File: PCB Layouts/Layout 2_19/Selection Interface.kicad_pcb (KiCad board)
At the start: 4 copper layers, 107.5 x 80 mm, 86 parts

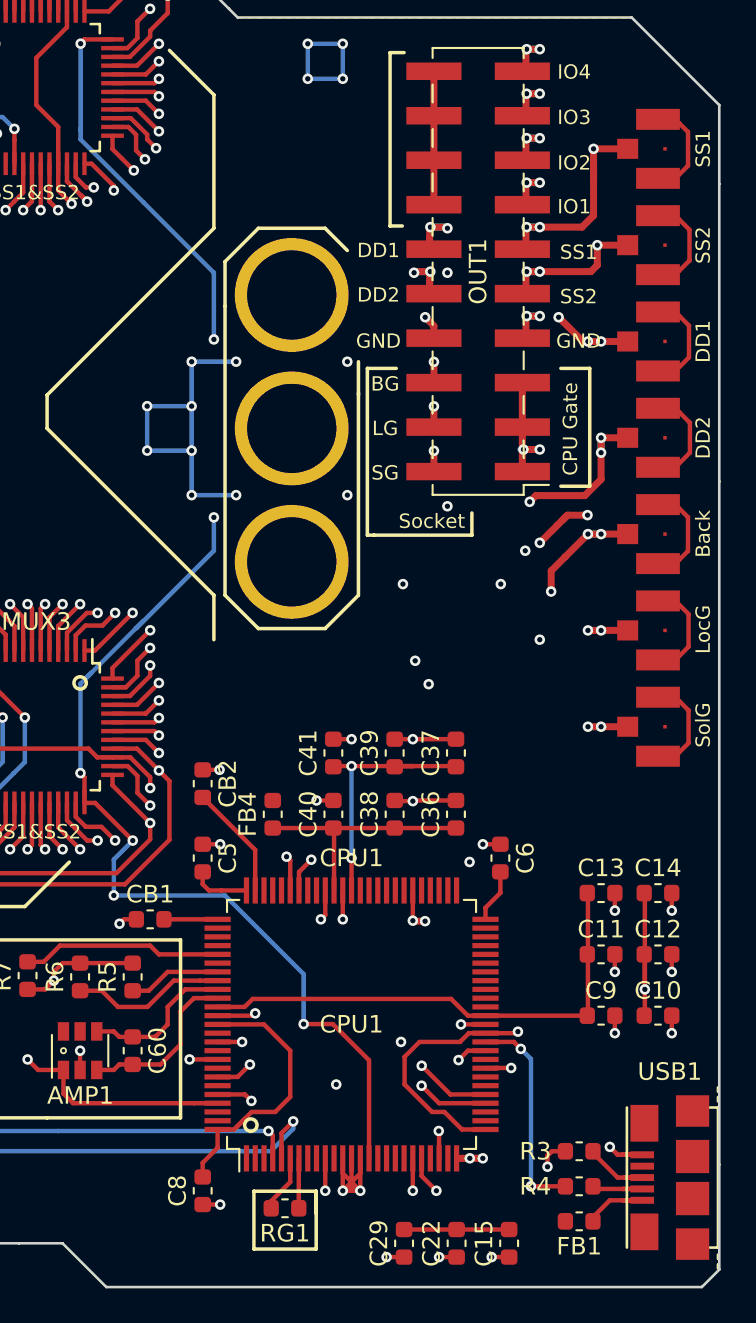
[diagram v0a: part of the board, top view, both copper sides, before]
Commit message: A few more tweaks to Layout 2_19 (very slightly moved up the USB port)
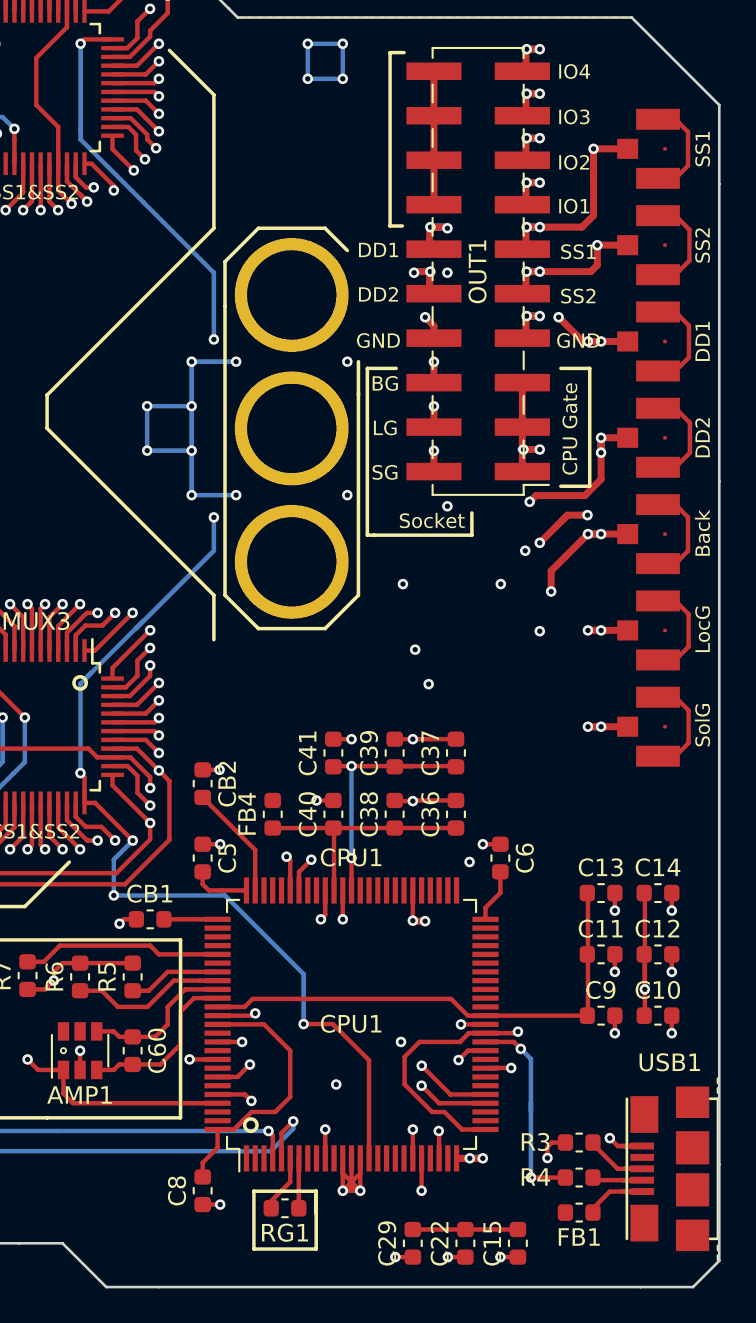
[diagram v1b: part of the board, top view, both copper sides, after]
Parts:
- moved C15 0.50 mm to (248.5, 147.5)
- moved C22 0.50 mm to (245.5, 147.5)
- moved C29 0.50 mm to (242.5, 147.5)
- moved FB1 0.50 mm to (252.0, 145.7)
- moved R3 0.50 mm to (252.0, 141.7)
- moved R4 0.50 mm to (252.0, 143.7)
- moved USB1 0.50 mm to (258.5, 143.2)
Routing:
- net SWDIO5: track 84.6 -> 87.0 mm
- net SWDCLK5: track 93.8 -> 92.6 mm
- net LocalGates_Socket: track 83.2 -> 82.4 mm
- net Gate: track 57.2 -> 56.7 mm
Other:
- outline, holes or cut-outs redrawn

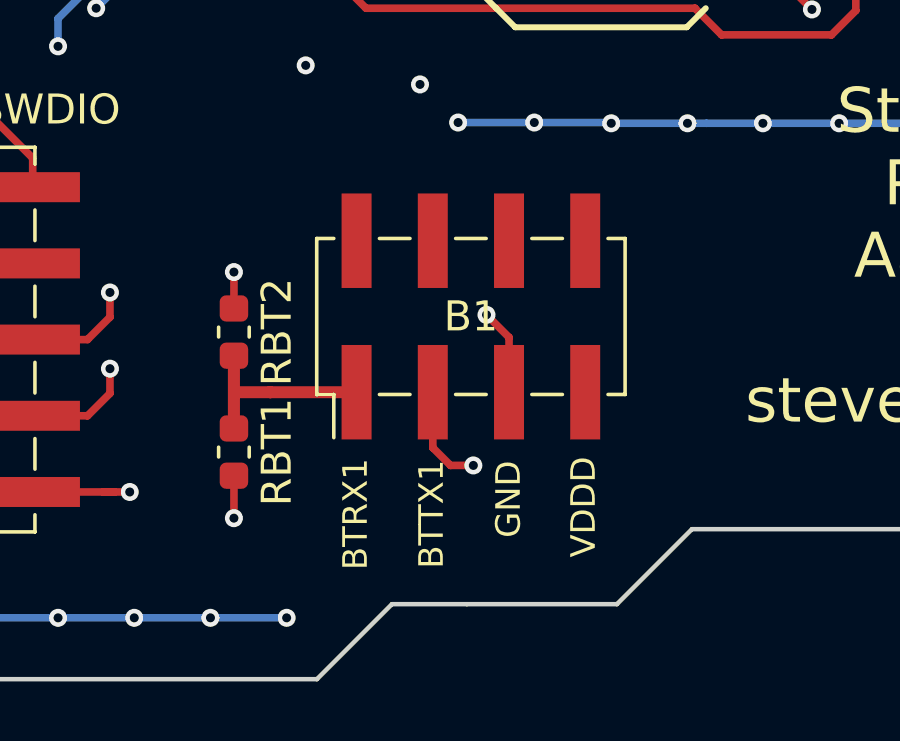
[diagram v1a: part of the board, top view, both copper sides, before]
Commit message: Rotated bluetooth header connector on Layout 2_19
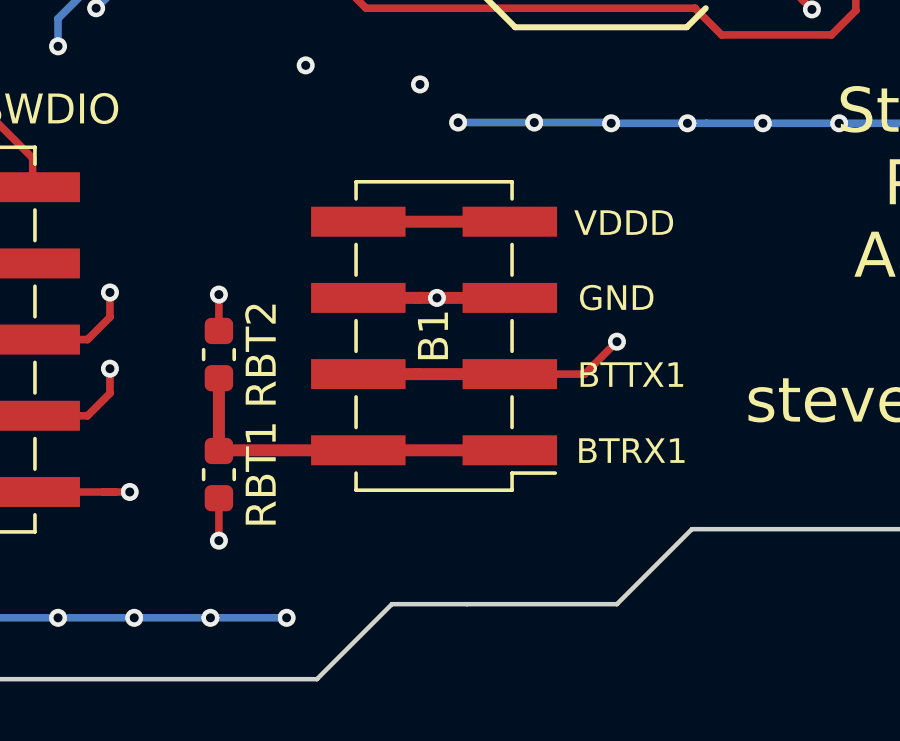
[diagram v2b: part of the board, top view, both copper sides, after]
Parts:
- moved B1 1.39 mm to (178.9, 138.6), turned to 180 degrees
- moved RBT1 0.90 mm to (171.7, 143.2)
- moved RBT2 0.90 mm to (171.7, 139.2)
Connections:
- B1 pad 2: Net-(B1-Pad2) -> BT1_RXR
- B1 pad 4: Net-(B1-Pad4) -> BT1_TX
- B1 pad 6: Net-(B1-Pad6) -> GND
- B1 pad 8: Net-(B1-Pad8) -> VDDD
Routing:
- net BT1_RXR: track 6.56 -> 12.1 mm
- net VDDD: track 130.8 -> 135.8 mm
- net GND: track 428.2 -> 430.3 mm
- net BT1_TX: track 81.1 -> 82.1 mm
- net BT1_RX: track 86.7 -> 87.3 mm

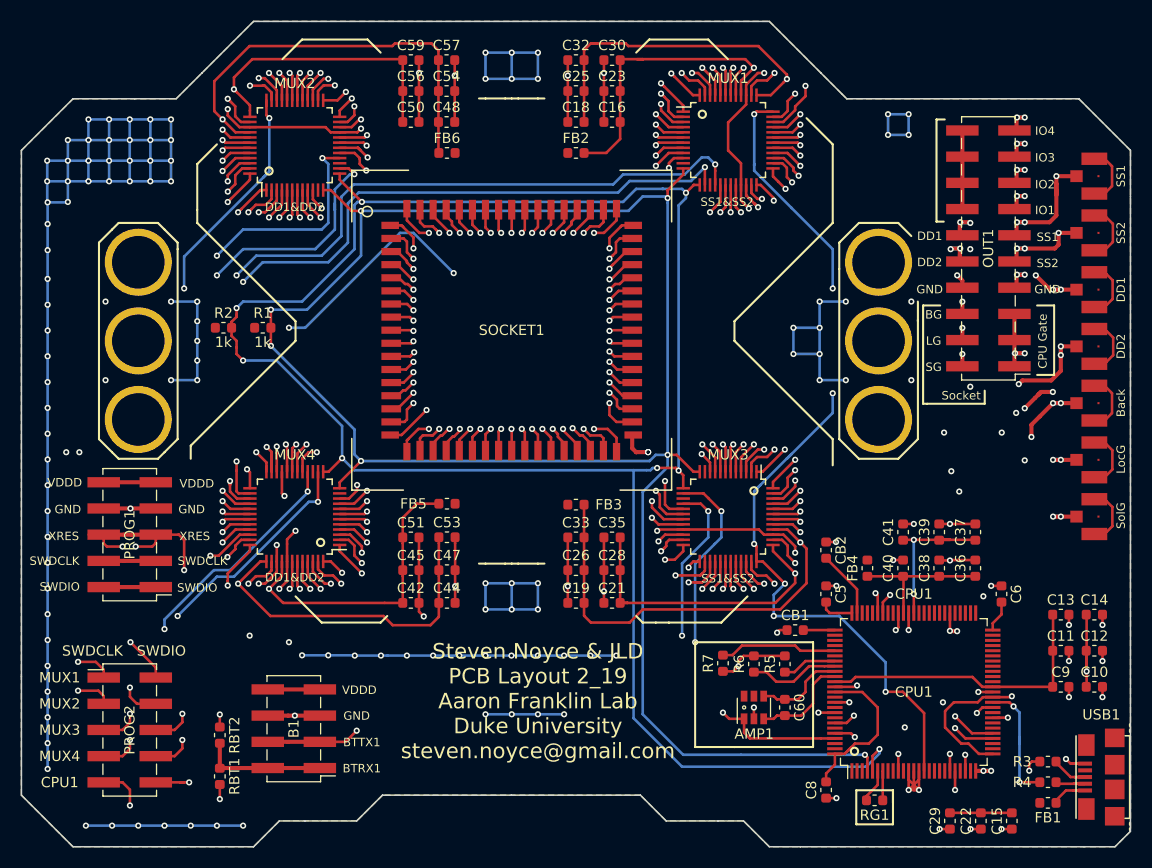
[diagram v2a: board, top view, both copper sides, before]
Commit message: Updates to Layout 2_19 (rearranged DD1 and DD2 signals to allow me to move up the bluetooth connector. Organized digital signals on the bottom side of the board. Slightly re-organized analog bus area to make room for moving the CPU up and to the right)
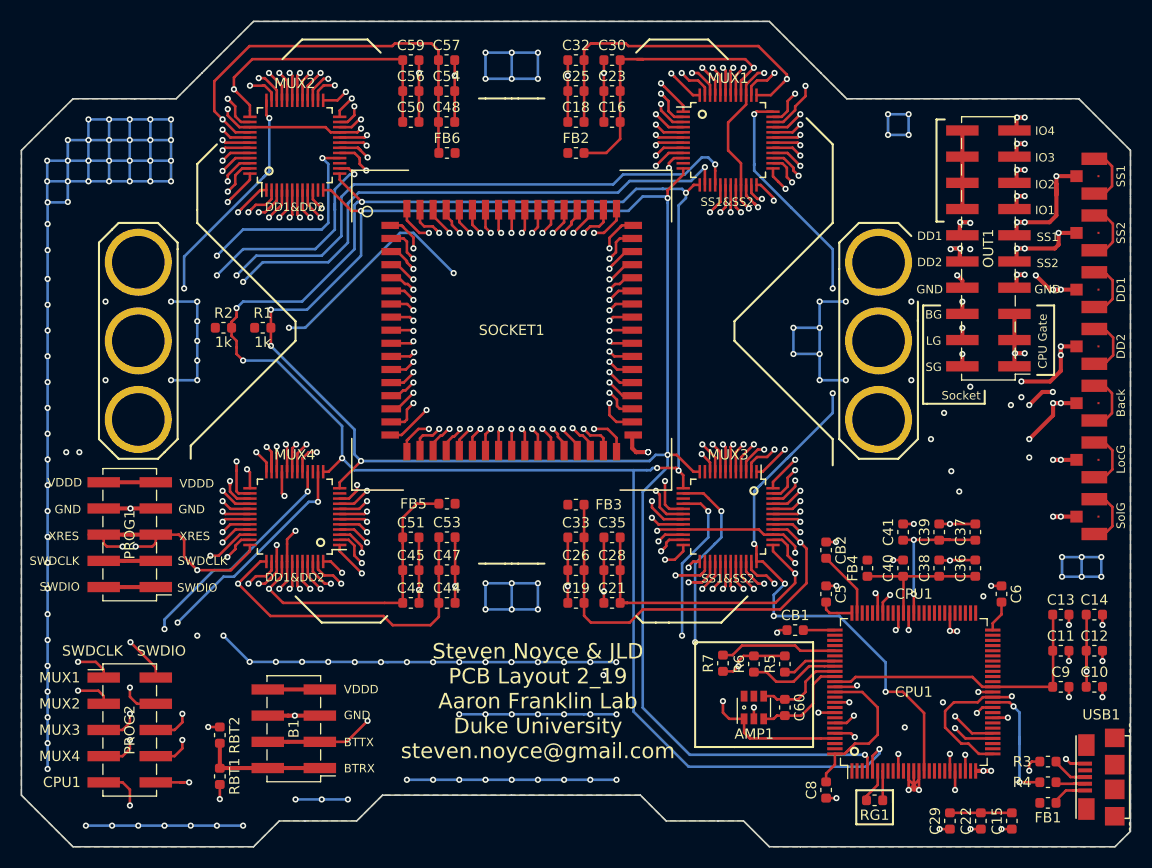
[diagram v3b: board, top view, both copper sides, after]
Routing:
- net GND: track 430.3 -> 483.7 mm, vias 164 -> 188
- net XRES: track 220.1 -> 228.7 mm, vias 13 -> 14
- net SWDIO3: track 77.3 -> 74.4 mm, vias 4 -> 3
- net SWDCLK3: track 78.0 -> 76.2 mm, vias 4 -> 3
- net DD2: track 235.6 -> 234.4 mm
- net SWDIO5: track 87.0 -> 88.1 mm
- net BT1_RX: track 87.3 -> 88.3 mm
- net SWDCLK5: track 92.6 -> 93.7 mm
- net BT1_TX: track 82.1 -> 82.9 mm
- net SWDIO4: track 37.8 -> 37.1 mm
- net BackGate_Socket: track 70.5 -> 69.9 mm, vias 6 -> 7
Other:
- board text added: "BTRX"
- board text added: "BTTX"
- board text removed: "BTRX1"
- board text removed: "BTTX1"

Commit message: Modified Layout 2_19 by shifting CPU1 up and to the right
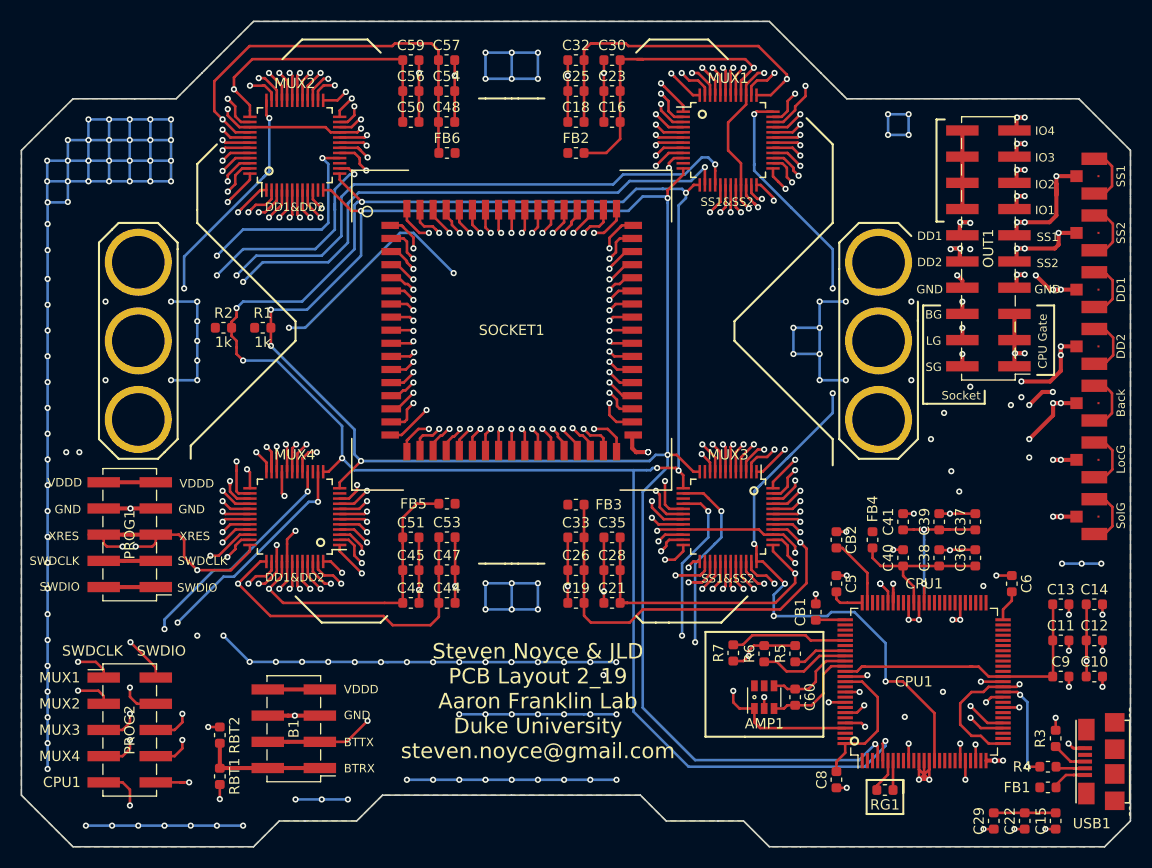
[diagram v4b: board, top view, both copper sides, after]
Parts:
- moved C15 4.25 mm to (252.8, 147.5)
- moved C22 4.25 mm to (249.8, 147.5)
- moved C29 4.25 mm to (246.8, 147.5)
- moved FB4 2.80 mm to (235.0, 120.2)
- moved CB1 2.66 mm to (229.5, 127.2), turned to 270 degrees
- moved R3 2.37 mm to (252.8, 139.5), turned to 270 degrees
- moved FB1 1.50 mm to (252.0, 144.2)
- moved R4 1.50 mm to (252.0, 142.2)
- moved USB1 1.50 mm to (258.5, 141.7)
- moved AMP1 1.41 mm to (224.5, 135.5)
- moved C5 1.41 mm to (231.5, 124.5)
- moved C6 1.41 mm to (248.5, 124.5)
- moved C60 1.41 mm to (227.5, 135.5)
- moved C8 1.41 mm to (231.5, 143.5)
- moved CB2 1.41 mm to (231.5, 120.2)
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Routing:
- net GND: track 483.7 -> 475.6 mm, vias 188 -> 185
- net Gate: track 56.7 -> 52.9 mm
- net VDDD: track 135.8 -> 132.4 mm
- net SS2: track 121.3 -> 118.3 mm
- net SS1: track 132.1 -> 129.5 mm
- net BT1_RX: track 88.3 -> 90.8 mm
- net USBDM_C1: track 12.3 -> 10.2 mm
- net USBDP_C1: track 12.5 -> 10.4 mm
- net I2C0_SCL: track 184.7 -> 186.5 mm
- net IO1: track 61.2 -> 59.6 mm
- net BT1_TX: track 82.9 -> 84.3 mm
- net IO3: track 62.1 -> 60.7 mm, vias 3 -> 4
- net DD1: track 241.2 -> 239.9 mm
- net VDDA_C1: track 14.1 -> 15.3 mm
- net VCCA_C1: track 15.1 -> 16.1 mm
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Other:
- outline, holes or cut-outs redrawn

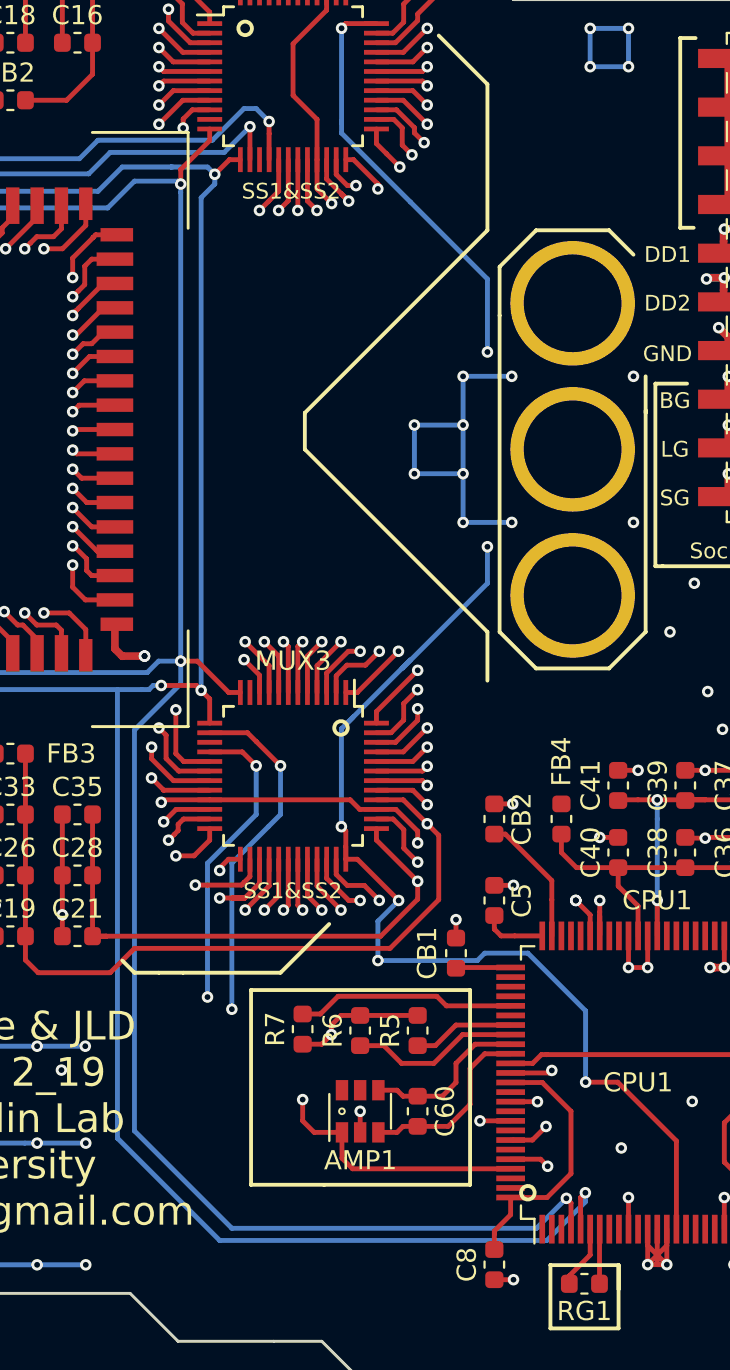
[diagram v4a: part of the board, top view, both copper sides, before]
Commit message: Cleaned up some signal routing on Layout 2_19
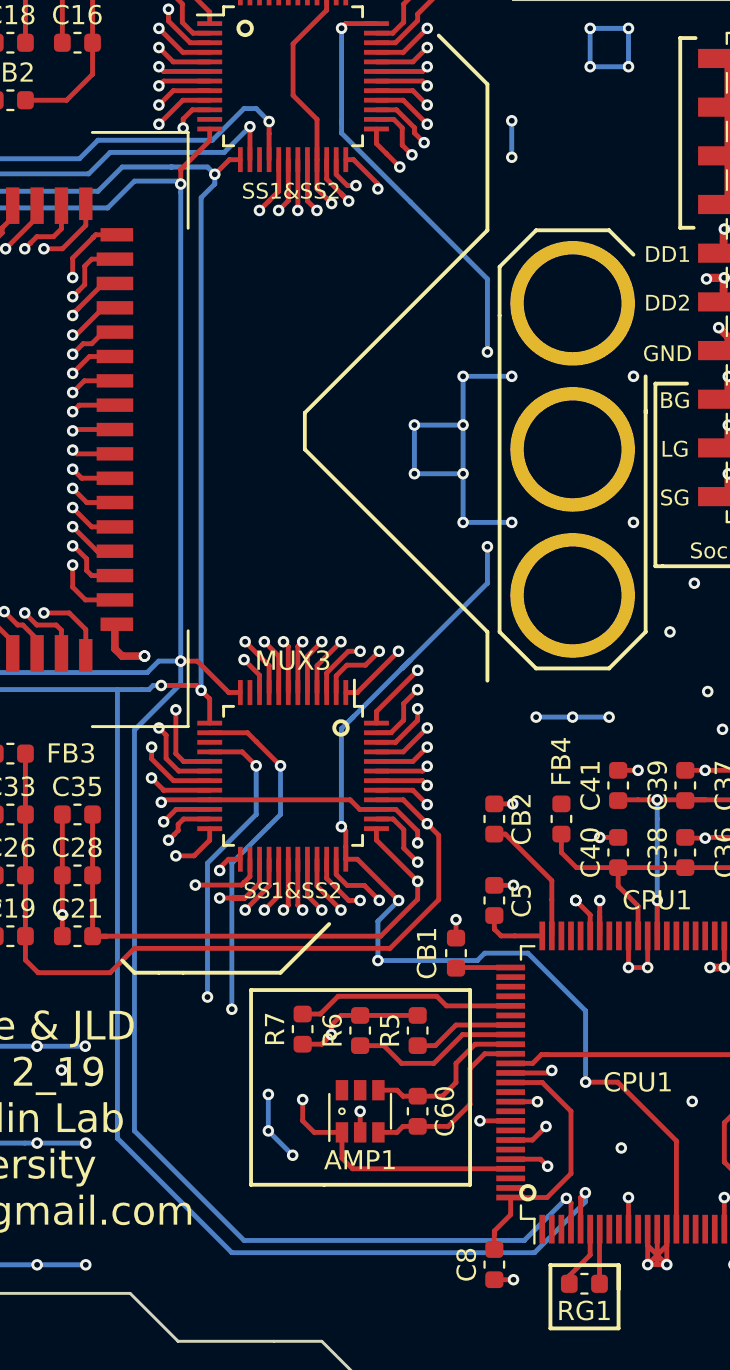
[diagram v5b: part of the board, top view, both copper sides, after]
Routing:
- net GND: track 475.6 -> 485.0 mm, vias 185 -> 193
- net I2C0_SCL: track 186.5 -> 187.1 mm
- net I2C0_SDA: track 196.4 -> 196.9 mm
